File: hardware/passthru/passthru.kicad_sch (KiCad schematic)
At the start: 79 parts, among them J1 ARM_SWD, J2 RJ45_LED_Shielded, J3 Screw_Terminal_01x02, Q1 Q_PMOS_DGS, Q2 Q_PMOS_DGS, Q3 Q_NPN_BEC, U1 EFM32GG11B8xx, U2 KSZ8081RND, U3 LM5085, U4 TPS2375-1

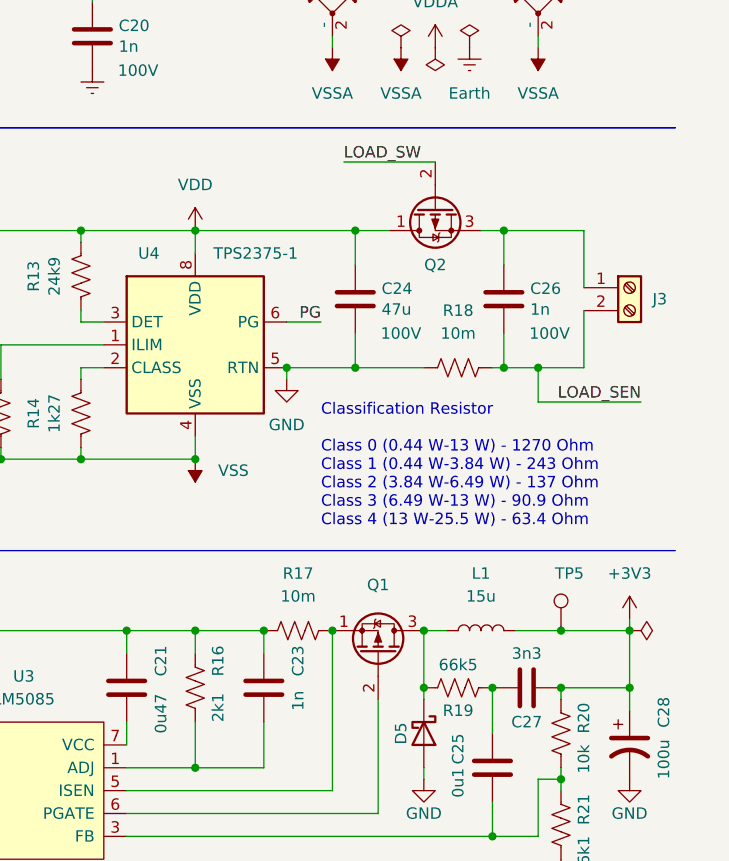
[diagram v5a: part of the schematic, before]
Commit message: passthru: update FETs to Si7465
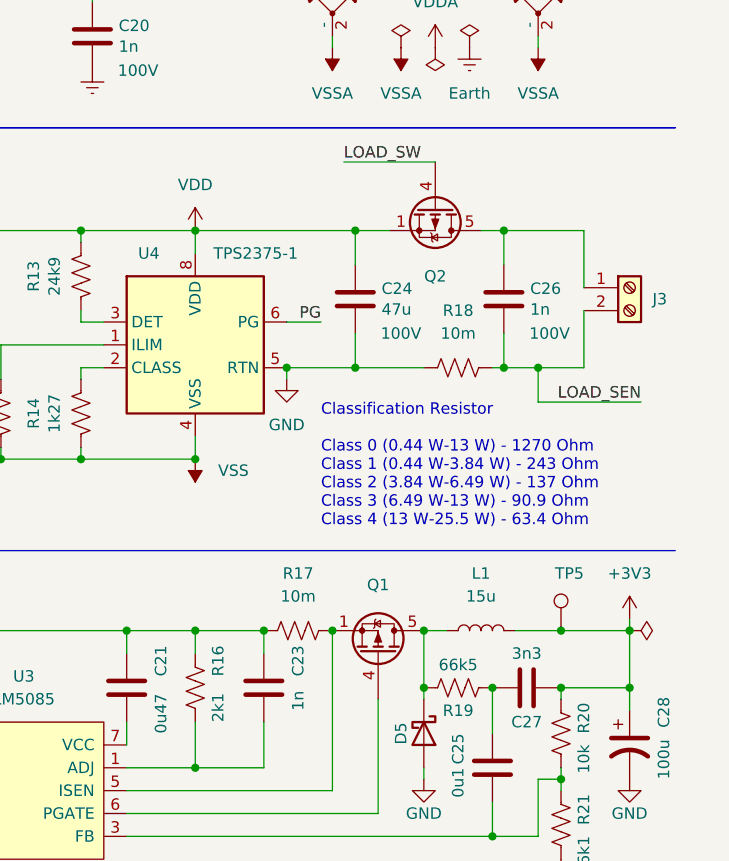
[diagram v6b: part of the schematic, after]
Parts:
- Q1: symbol Device:Q_PMOS_SGD -> common:Si7465DP
- Q2: symbol Device:Q_PMOS_DGS -> common:Si7465DP
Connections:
- net LOAD_SW: now also Q2.4 (G); no longer Q2.2 (G)
- net VDD: now also Q2.2 (S), Q2.3 (S)
- net at D5.1 (K), L1.1, R19.2: now also Q1.5 (D); no longer Q1.3 (D)
- net at C26.1, J3.1 (Pin_1): now also Q2.5 (D); no longer Q2.3 (S)
- net at Q1.1 (S), R17.2, U3.5 (ISEN): now also Q1.2 (S), Q1.3 (S)
- net at U3.6 (PGATE): now also Q1.4 (G); no longer Q1.2 (G)
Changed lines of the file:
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@@
     (pin "2")
   )
-  (symbol (lib_id "Device:Q_PMOS_SGD") (at 232.41 142.24 270) (mirror x) (unit 1)
+  (symbol (lib_id "common:Si7465DP") (at 232.41 140.97 90) (unit 1)
     (in_bom yes) (on_board yes) (fields_autoplaced)
     (property "Reference" "Q1" (id 0) (at 232.41 134.62 90))
-    (property "Value" "Q_PMOS_DGS" (id 1) (at 233.6799 135.89 0)
+    (property "Value" "Q_PMOS_DGS" (id 1) (at 231.1401 134.62 0)
       (effects (font (size 1.27 1.27)) (justify left) hide)
     )
-    (property "Footprint" "Package_SO:PowerPAK_SO-8_Single" (id 2) (at 234.95 137.16 0)
-      (effects (font (size 1.27 1.27)) hide)
-    )
-    (property "Datasheet" "~" (id 3) (at 232.41 142.24 0)
-      (effects (font (size 1.27 1.27)) hide)
+    (property "Footprint" "Package_SO:PowerPAK_SO-8_Single" (id 2) (at 234.315 135.89 0)
+      (effects (font (size 1.27 1.27) italic) (justify left) hide)
+    )
+    (property "Datasheet" "~" (id 3) (at 232.41 140.97 0)
+      (effects (font (size 1.27 1.27)) (justify left) hide)
     )
     (pin "1")
     (pin "2")
     (pin "3")
+    (pin "4")
+    (pin "5")
   )
   (symbol (lib_id "Device:R_US") (at 31.75 57.15 0) (unit 1)
@@
     (pin "1")
   )
-  (symbol (lib_id "Device:Q_PMOS_DGS") (at 238.76 92.71 90) (mirror x) (unit 1)
-    (in_bom yes) (on_board yes)
-    (property "Reference" "Q2" (id 0) (at 238.76 99.06 90))
-    (property "Value" "Q_PMOS_DGS" (id 1) (at 238.76 102.87 90)
-      (effects (font (size 1.27 1.27)) hide)
-    )
-    (property "Footprint" "Package_SO:PowerPAK_SO-8_Single" (id 2) (at 236.22 97.79 0)
-      (effects (font (size 1.27 1.27)) hide)
-    )
-    (property "Datasheet" "~" (id 3) (at 238.76 92.71 0)
-      (effects (font (size 1.27 1.27)) hide)
+  (symbol (lib_id "common:Si7465DP") (at 238.76 93.98 90) (mirror x) (unit 1)
+    (in_bom yes) (on_board yes)
+    (property "Reference" "Q2" (id 0) (at 238.76 100.33 90))
+    (property "Value" "Q_PMOS_DGS" (id 1) (at 238.76 104.14 90)
+      (effects (font (size 1.27 1.27)) hide)
+    )
+    (property "Footprint" "Package_SO:PowerPAK_SO-8_Single" (id 2) (at 240.665 99.06 0)
+      (effects (font (size 1.27 1.27) italic) (justify left) hide)
+    )
+    (property "Datasheet" "~" (id 3) (at 238.76 93.98 0)
+      (effects (font (size 1.27 1.27)) (justify left) hide)
     )
     (pin "1")
     (pin "2")
     (pin "3")
+    (pin "4")
+    (pin "5")
   )
   (symbol (lib_id "Device:C") (at 246.38 102.87 0) (unit 1)

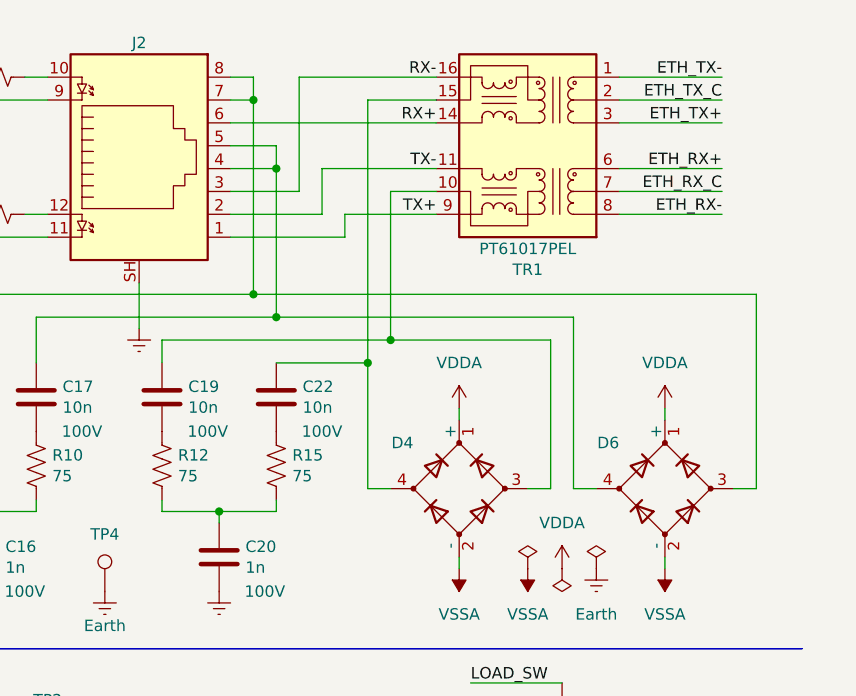
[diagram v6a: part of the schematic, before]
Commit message: passthru: flip magnetics to make routing easier
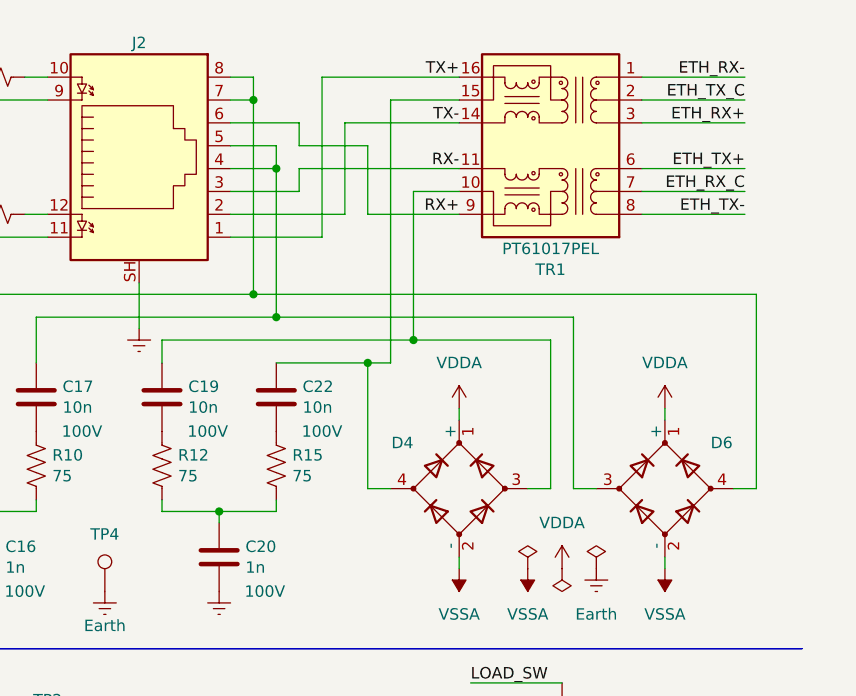
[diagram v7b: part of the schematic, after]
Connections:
- net ETH_RX+: now also TR1.3 (TD-); no longer TR1.6 (RD+)
- net ETH_RX-: now also TR1.1 (TD+); no longer TR1.8 (RD-)
- net ETH_TX+: now also TR1.6 (RD+); no longer TR1.3 (TD-)
- net ETH_TX-: now also TR1.8 (RD-); no longer TR1.1 (TD+)
- net RX+: now also TR1.9 (RX-); no longer TR1.14 (TX-)
- net RX-: now also TR1.11 (RX+); no longer TR1.16 (TX+)
- net TX+: now also TR1.16 (TX+); no longer TR1.9 (RX-)
- net TX-: now also TR1.14 (TX-); no longer TR1.11 (RX+)
- net at C17.1, J2.4, J2.5: now also D6.3; no longer D6.4
- net at C14.1, J2.7, J2.8: now also D6.4; no longer D6.3
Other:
- moved on the sheet: D6, TR1

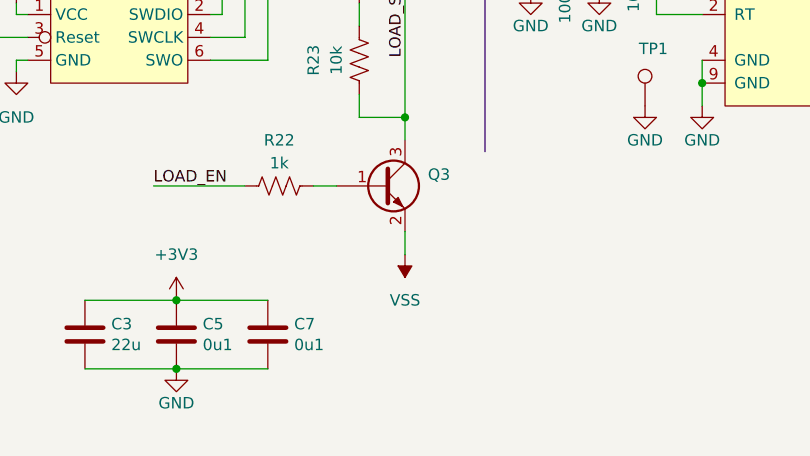
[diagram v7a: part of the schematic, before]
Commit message: passthru: ground the load switch through the PoE bypass FET
This will prevent the load from being enabled until the PoE
negotiation has completed. It also makes routing a little easier.
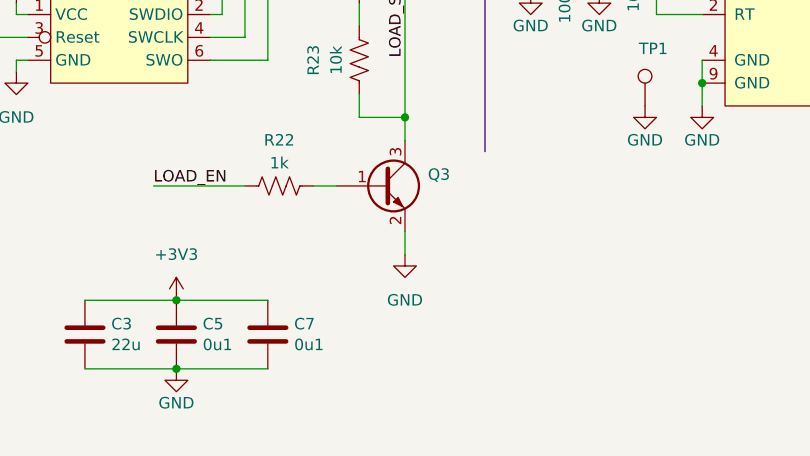
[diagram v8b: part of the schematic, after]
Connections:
- net GND: now also Q3.2 (E)
- net VSS: no longer Q3.2 (E)
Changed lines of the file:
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@@
     (pin "2")
-  )
-  (symbol (lib_id "power:VSS") (at 148.59 181.61 180) (unit 1)
-    (in_bom yes) (on_board yes) (fields_autoplaced)
-    (property "Reference" "#PWR053" (id 0) (at 148.59 177.8 0)
-      (effects (font (size 1.27 1.27)) hide)
-    )
-    (property "Value" "VSS" (id 1) (at 148.59 186.69 0))
-    (property "Footprint" "" (id 2) (at 148.59 181.61 0)
-      (effects (font (size 1.27 1.27)) hide)
-    )
-    (property "Datasheet" "" (id 3) (at 148.59 181.61 0)
-      (effects (font (size 1.27 1.27)) hide)
-    )
-    (pin "1")
   )
   (symbol (lib_id "Device:R_US") (at 194.31 63.5 0) (unit 1)
@@
     (pin "1")
   )
+  (symbol (lib_id "power:GND") (at 148.59 181.61 0) (unit 1)
+    (in_bom yes) (on_board yes) (fields_autoplaced)
+    (property "Reference" "#PWR0101" (id 0) (at 148.59 187.96 0)
+      (effects (font (size 1.27 1.27)) hide)
+    )
+    (property "Value" "GND" (id 1) (at 148.59 186.69 0))
+    (property "Footprint" "" (id 2) (at 148.59 181.61 0)
+      (effects (font (size 1.27 1.27)) hide)
+    )
+    (property "Datasheet" "" (id 3) (at 148.59 181.61 0)
+      (effects (font (size 1.27 1.27)) hide)
+    )
+    (pin "1")
+  )
   (symbol (lib_id "power:GND") (at 113.03 41.91 0) (unit 1)
     (in_bom yes) (on_board yes)
@@
       (reference "#PWR052") (unit 1) (value "VDD") (footprint "")
     )
-    (path "/089f1e7c-a914-4a38-88f3-88413ac75afc"
-      (reference "#PWR053") (unit 1) (value "VSS") (footprint "")
+    (path "/daad9d13-ecc0-4c91-9861-8f109eef8381"
+      (reference "#PWR0101") (unit 1) (value "GND") (footprint "")
     )
     (path "/c61db7ba-41b9-4169-bb6f-11722db31004"
